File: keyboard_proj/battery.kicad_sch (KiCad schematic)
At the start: 17 parts, among them IC1 DW01A-G, IC2 TP4056-42-ESOP8, IC3 LD1117DT12CTR, Q1 FS8205A, Q2 2N7002, U7 SK12D07VG5, U9 1.0K-ES-4PWB

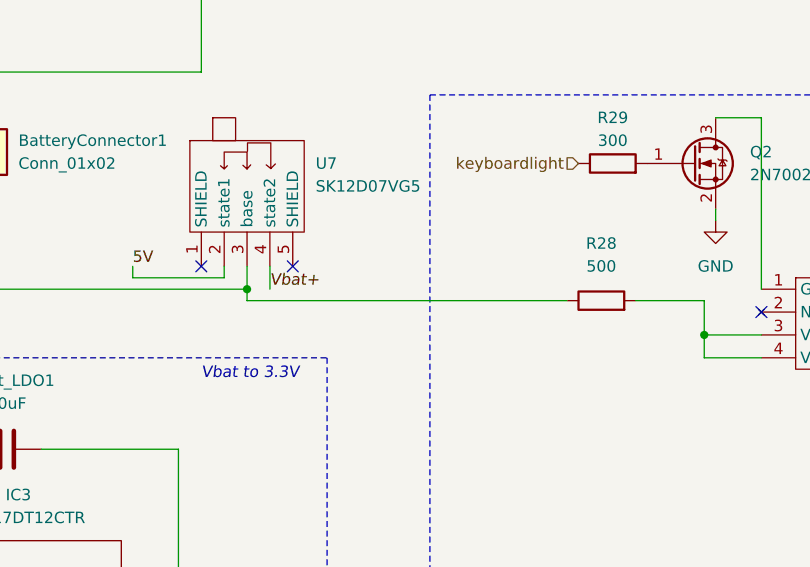
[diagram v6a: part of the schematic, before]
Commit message: Routing bientot fini check schematic et tout mettre sur la meme face
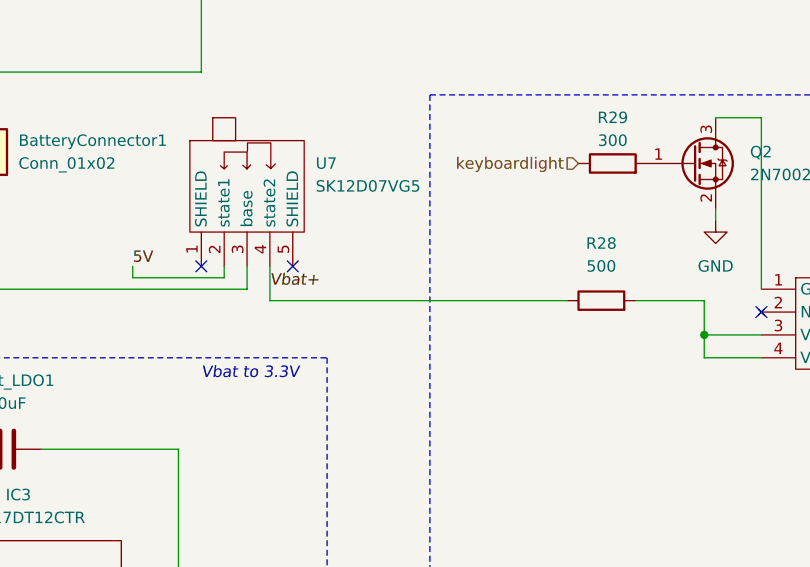
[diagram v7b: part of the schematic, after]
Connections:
- net +: no longer R28.1
- net Vbat+: now also R28.1
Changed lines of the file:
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@@
   (junction (at 176.53 52.07) (diameter 0) (color 0 0 0 0)
-  )
-  (junction (at 194.31 90.17) (diameter 0) (color 0 0 0 0)
   )
   (junction (at 176.53 44.45) (diameter 0) (color 0 0 0 0)
@@
   )
   (wire (pts (xy 186.69 107.95) (xy 186.69 123.19))
-    (stroke (width 0) (type default))
-  )
-  (wire (pts (xy 229.87 91.44) (xy 194.31 91.44))
     (stroke (width 0) (type default))
   )
@@
     (stroke (width 0) (type dash))
   )
+  (wire (pts (xy 229.87 91.44) (xy 196.85 91.44))
+    (stroke (width 0) (type default))
+  )
   (wire (pts (xy 130.81 39.37) (xy 132.08 39.37))
     (stroke (width 0) (type default))
   )
   (wire (pts (xy 152.4 107.95) (xy 152.4 120.65))
-    (stroke (width 0) (type default))
-  )
-  (wire (pts (xy 194.31 91.44) (xy 194.31 90.17))
     (stroke (width 0) (type default))
   )
@@
     (stroke (width 0) (type default))
   )
-  (wire (pts (xy 196.85 87.63) (xy 196.85 90.17))
+  (wire (pts (xy 196.85 87.63) (xy 196.85 91.44))
     (stroke (width 0) (type default))
   )

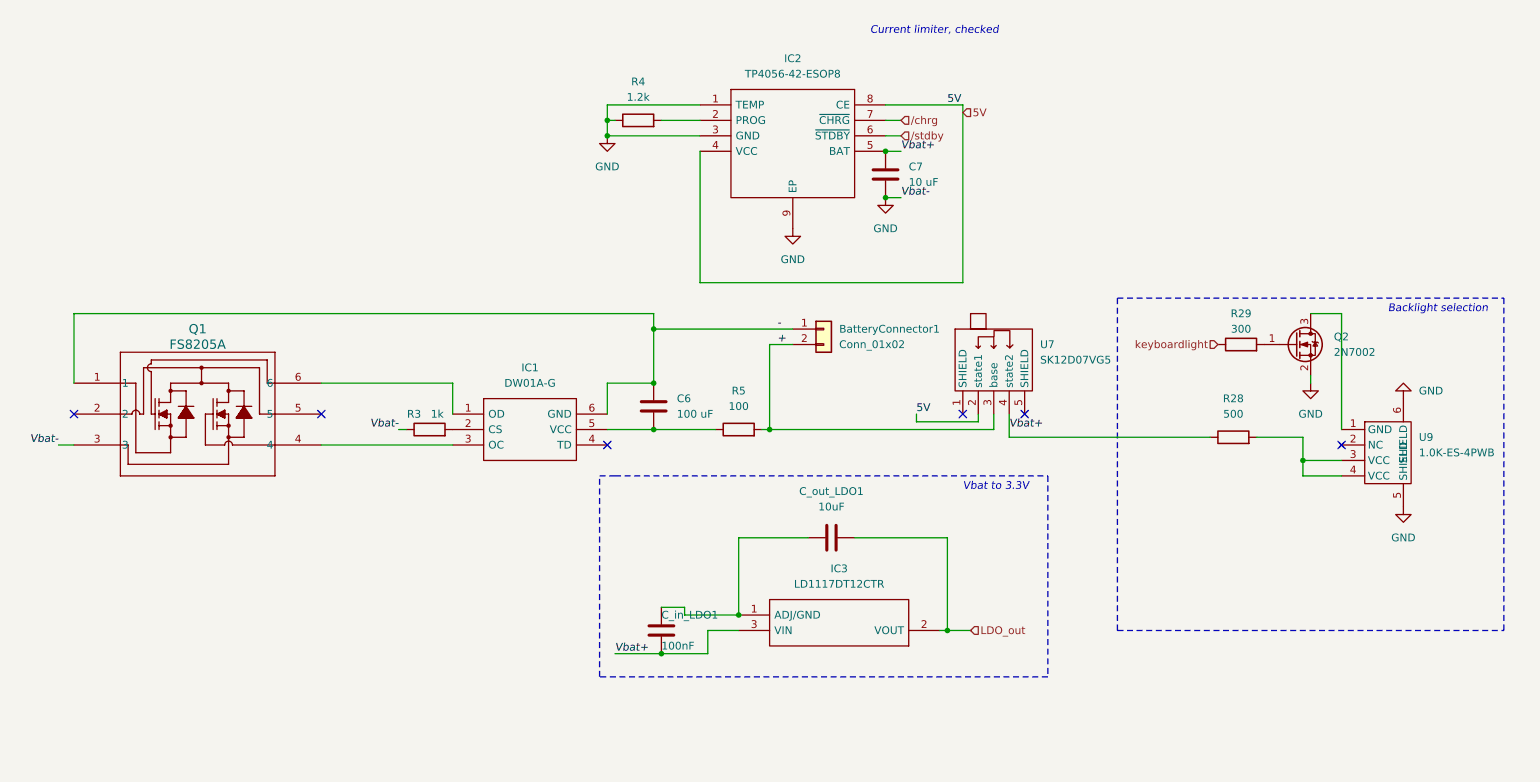
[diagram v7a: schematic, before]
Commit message: Power dlvry changée, ok mtn, routing updated
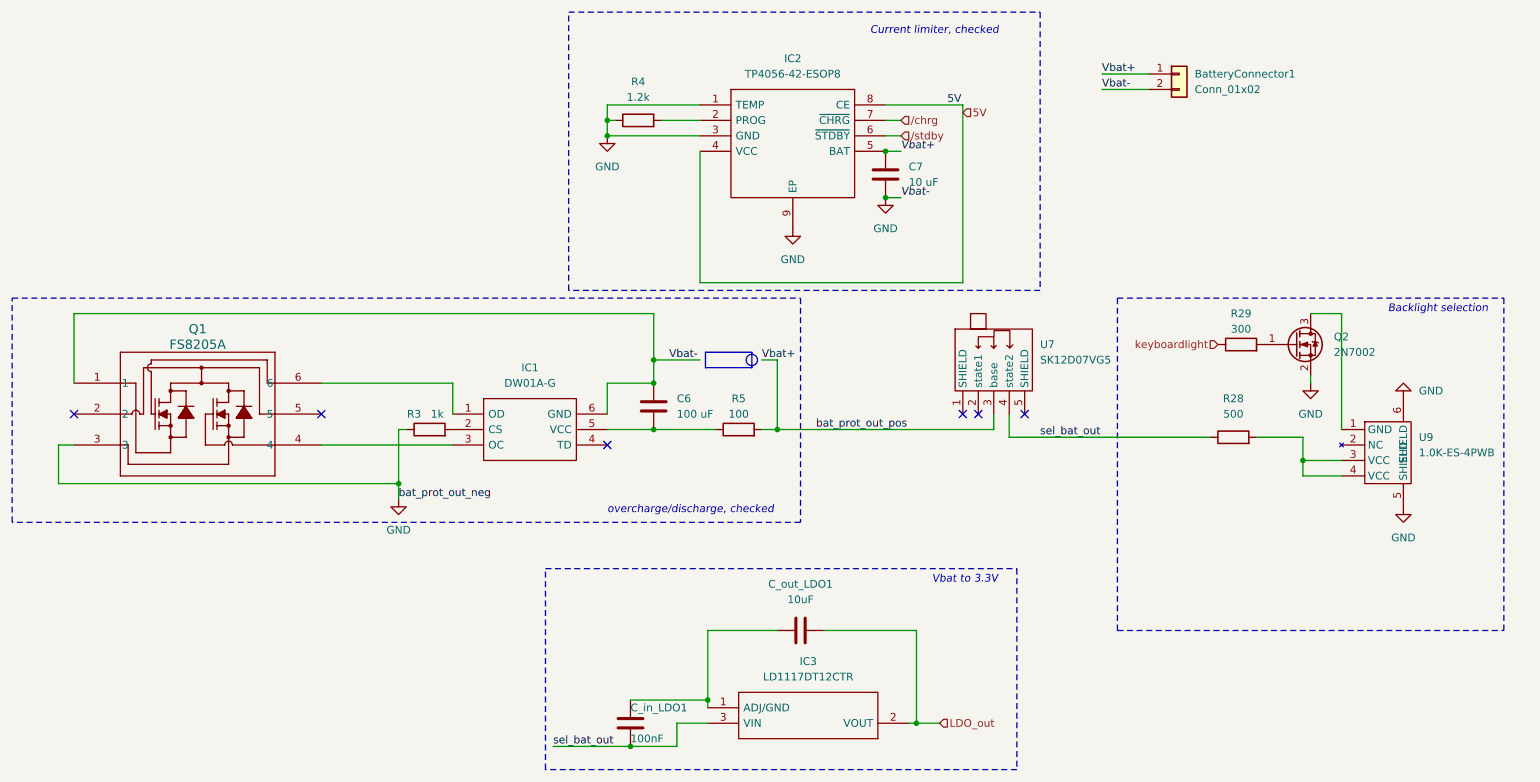
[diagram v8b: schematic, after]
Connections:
- net 5V: no longer U7.2 (state1)
- net GND: now also BatteryConnector1.2 (Pin_2), C6.1, IC1.6 (GND), Q1.1
- net Vbat+: now also BatteryConnector1.1 (Pin_1), R5.2, U7.3 (base); no longer C_in_LDO1.2, IC3.3 (VIN), R28.1, U7.4 (state2)
- removed net +: BatteryConnector1.2 (Pin_2), R5.2, U7.3 (base)
- removed net -: BatteryConnector1.1 (Pin_1), C6.1, IC1.6 (GND), Q1.1
- new net sel_bat_out: C_in_LDO1.2, IC3.3 (VIN), R28.1, U7.4 (state2)
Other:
- note added: "overcharge/discharge, checked"
- moved on the sheet: BatteryConnector1, C_in_LDO1, C_out_LDO1, IC3
